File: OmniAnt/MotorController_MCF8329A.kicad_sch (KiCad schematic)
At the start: 42 parts, among them J10 Conn_01x01, J12 Conn_01x01, J23 Conn_01x01, J26 Conn_01x01, J28 Conn_01x01, J30 Conn_01x01, J32 Conn_01x01, J34 Conn_01x01, J36 Conn_01x01, J38 Conn_01x01, J8 Conn_01x01, Q1 NTMFS4C324NT1G, Q3 NTMFS4C324NT1G, Q4 NTMFS4C324NT1G, Q5 NTMFS4C324NT1G, Q6 NTMFS4C324NT1G, U4 MCF8329A1IREER

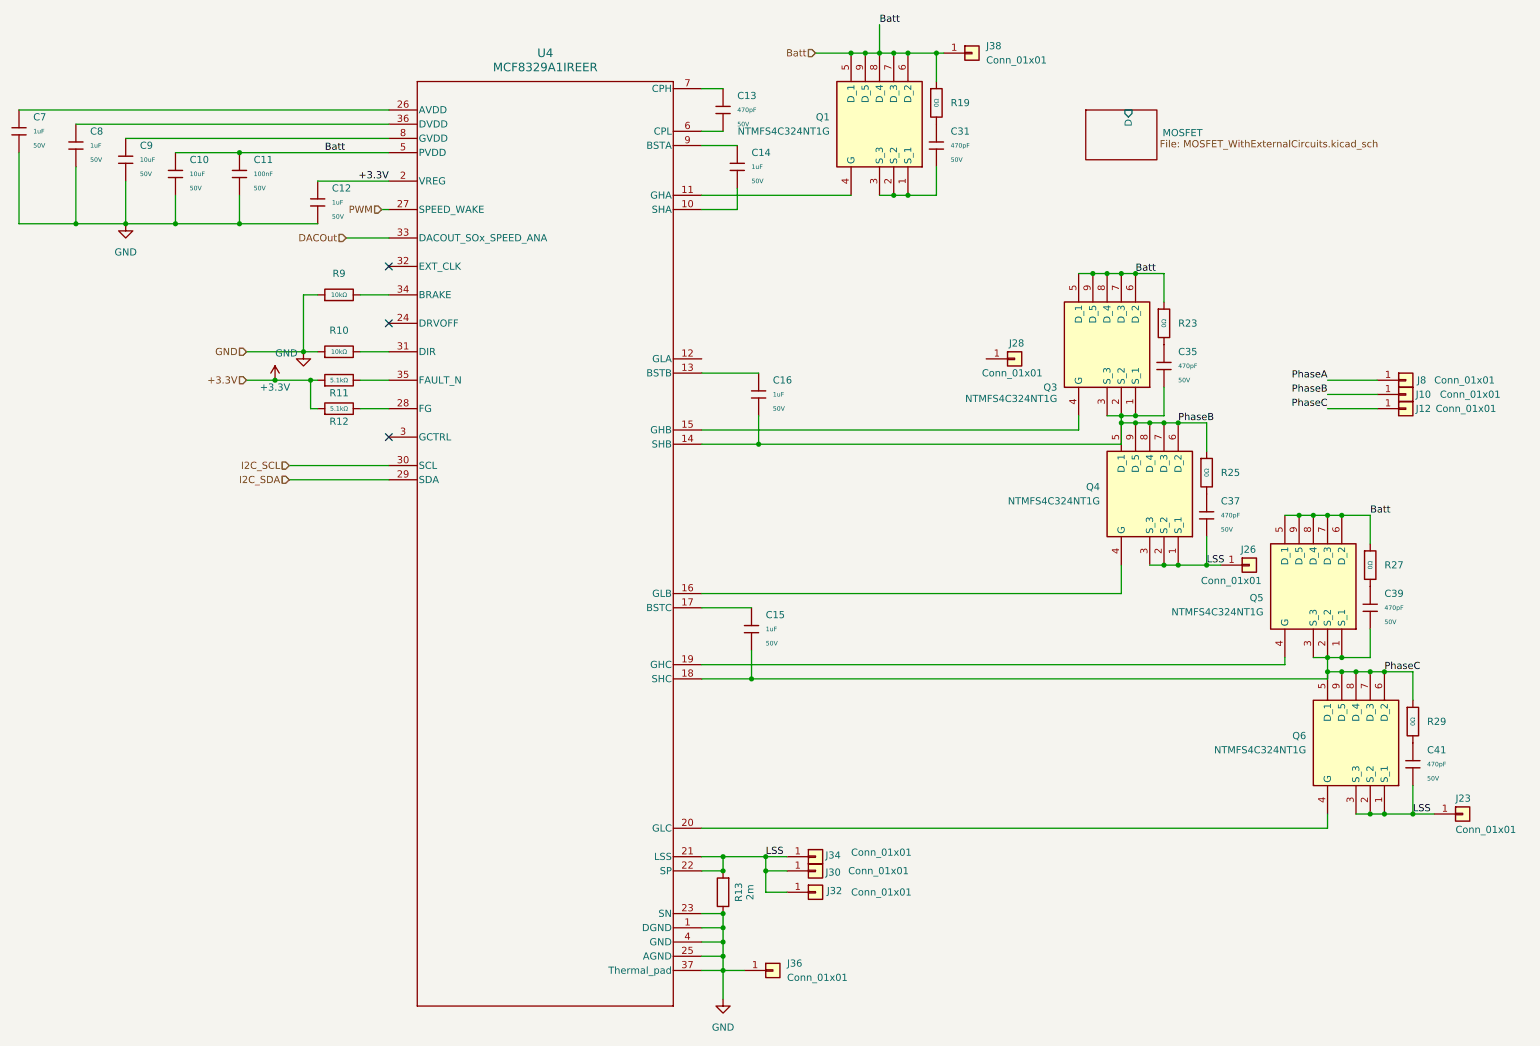
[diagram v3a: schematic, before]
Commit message: I got the mosfets in as a separate sheet and selected the additional protection circuitry. I'm working on finding the other recommended capacitors now.
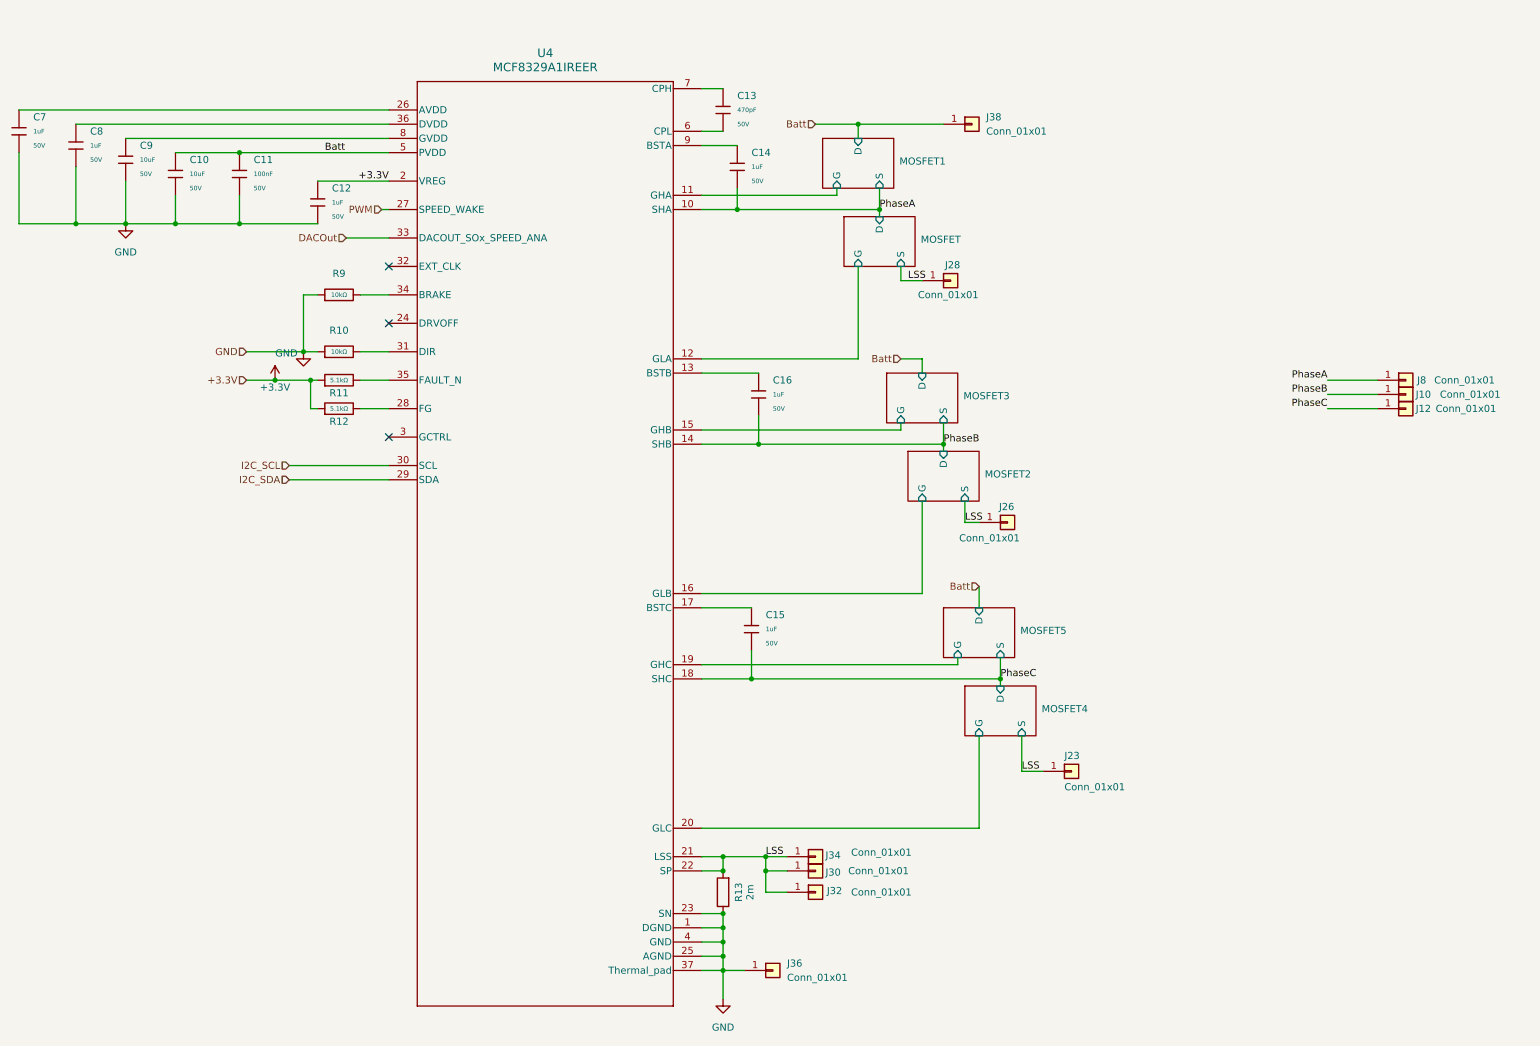
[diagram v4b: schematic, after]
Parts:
- removed C31, C35, C37, C39, C41: 470pF, PCM_JLCPCB:C_0603, symbol PCM_JLCPCB-Capacitors:0603,470pF
- removed Q1, Q3, Q4, Q5, Q6: NTMFS4C324NT1G, Footprints:NVMFS5C442NLWFAFT1G, symbol NTMFS4C324NT1G:NTMFS4C324NT1G
- removed R19, R23, R25, R27, R29: 0Ω, PCM_JLCPCB:R_0402, symbol PCM_JLCPCB-Resistors:0402,0Ω
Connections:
- net LSS: now also J28.1 (Pin_1)
- net PhaseA: now also C14.2, U4.10 (SHA)
- net MOSFET2/G: now reaches U4.16 (GLB)
- net MOSFET4/G: now reaches U4.20 (GLC)
- net MOSFET1/G: now reaches U4.11 (GHA)
- net MOSFET5/G: now reaches U4.19 (GHC)
- net MOSFET3/G: now reaches U4.15 (GHB)
- net MOSFET/G: now reaches U4.12 (GLA)
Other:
- added sheet MOSFET1 (MOSFET_WithExternalCircuits.kicad_sch)
- added sheet MOSFET2 (MOSFET_WithExternalCircuits.kicad_sch)
- added sheet MOSFET3 (MOSFET_WithExternalCircuits.kicad_sch)
- added sheet MOSFET4 (MOSFET_WithExternalCircuits.kicad_sch)
- added sheet MOSFET5 (MOSFET_WithExternalCircuits.kicad_sch)
- sheet MOSFET ports: added G, S; removed none
- moved on the sheet: J23, J26, J28, J38

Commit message: Well shit making the FETs into libraries totally screwed up the annotation :( I decided to just redo the layout for the FETs anyhow.
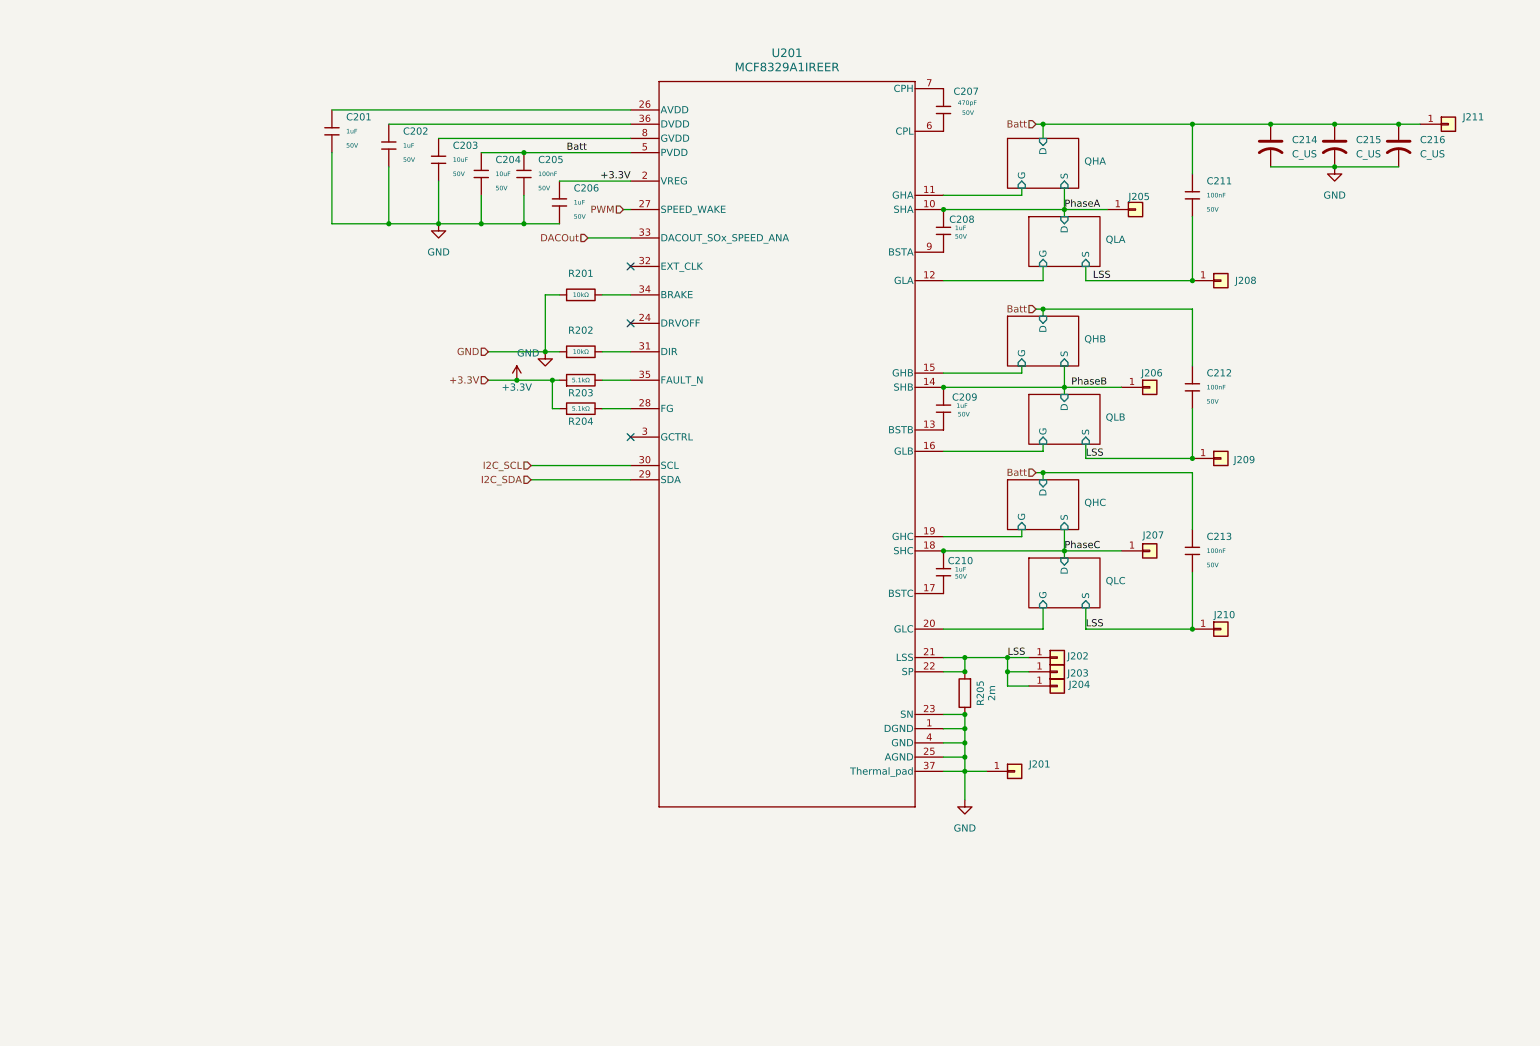
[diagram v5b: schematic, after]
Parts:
- added C211, C212, C213: 100nF, PCM_JLCPCB:C_0603, symbol PCM_JLCPCB-Capacitors:0603,100nF
- added C214, C215, C216: C_US, Capacitor_THT:CP_Radial_D6.3mm_P2.50mm, symbol Device:C_US
- C201: renamed from C7; Stock 16297537 -> 17190513
- C202: renamed from C8; Stock 16297537 -> 17190513
- C203: renamed from C9; Stock 1551376 -> 1647341
- C204: renamed from C10; Stock 1551376 -> 1647341
- C205: renamed from C11; Stock 58347526 -> 64667839
- C206: renamed from C12; Stock 16297537 -> 17190513
- C207: renamed from C13; Stock 611581 -> 676425
- C208: renamed from C14; Stock 16297537 -> 17190513
- C209: renamed from C16; Stock 16297537 -> 17190513
- C210: renamed from C15; Stock 16297537 -> 17190513
- R201: renamed from R9; Stock 16030120 -> 17848646
- R202: renamed from R10; Stock 16030120 -> 17848646
- R203: renamed from R11; Stock 4254023 -> 4532170
- R204: renamed from R12; Stock 4254023 -> 4532170
- renumbered J36 to J201, J34 to J202, J30 to J203, J32 to J204, J8 to J205, J10 to J206, J12 to J207, J28 to J208, J26 to J209, J23 to J210, J38 to J211, R13 to R205, U4 to U201
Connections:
- net Batt: now also C211.1, C212.1, C213.1, C214.1, C215.1, C216.1
- net GND: now also C214.2, C215.2, C216.2
- net LSS: now also C211.2, C212.2, C213.2
- net PhaseA: now also C208.1; no longer C208.2
- net PhaseB: now also C209.1; no longer C209.2
- net PhaseC: now also C210.1; no longer C210.2
- net at U201.9 (BSTA): now also C208.2; no longer C208.1
- net at U201.13 (BSTB): now also C209.2; no longer C209.1
- net at U201.17 (BSTC): now also C210.2; no longer C210.1
- net MOSFET/G renamed QLA/G
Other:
- sheet MOSFET1 renamed QHA
- sheet MOSFET2 renamed QLB
- sheet MOSFET3 renamed QHB
- sheet MOSFET4 renamed QLC
- sheet MOSFET5 renamed QHC
- removed sheet MOSFET
- added sheet QLA (MOSFET_WithExternalCircuits.kicad_sch)
- moved on the sheet: C201, C202, C203, C204, C205, C206, C207, C208, C209, C210, J201, J202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
